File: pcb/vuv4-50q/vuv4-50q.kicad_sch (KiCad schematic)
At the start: 7 parts, among them J1 Conn_Coaxial, J2 Conn_Coaxial, J3 Conn_Coaxial, J4 Conn_Coaxial, J5 Conn_Coaxial, U1 SiPM

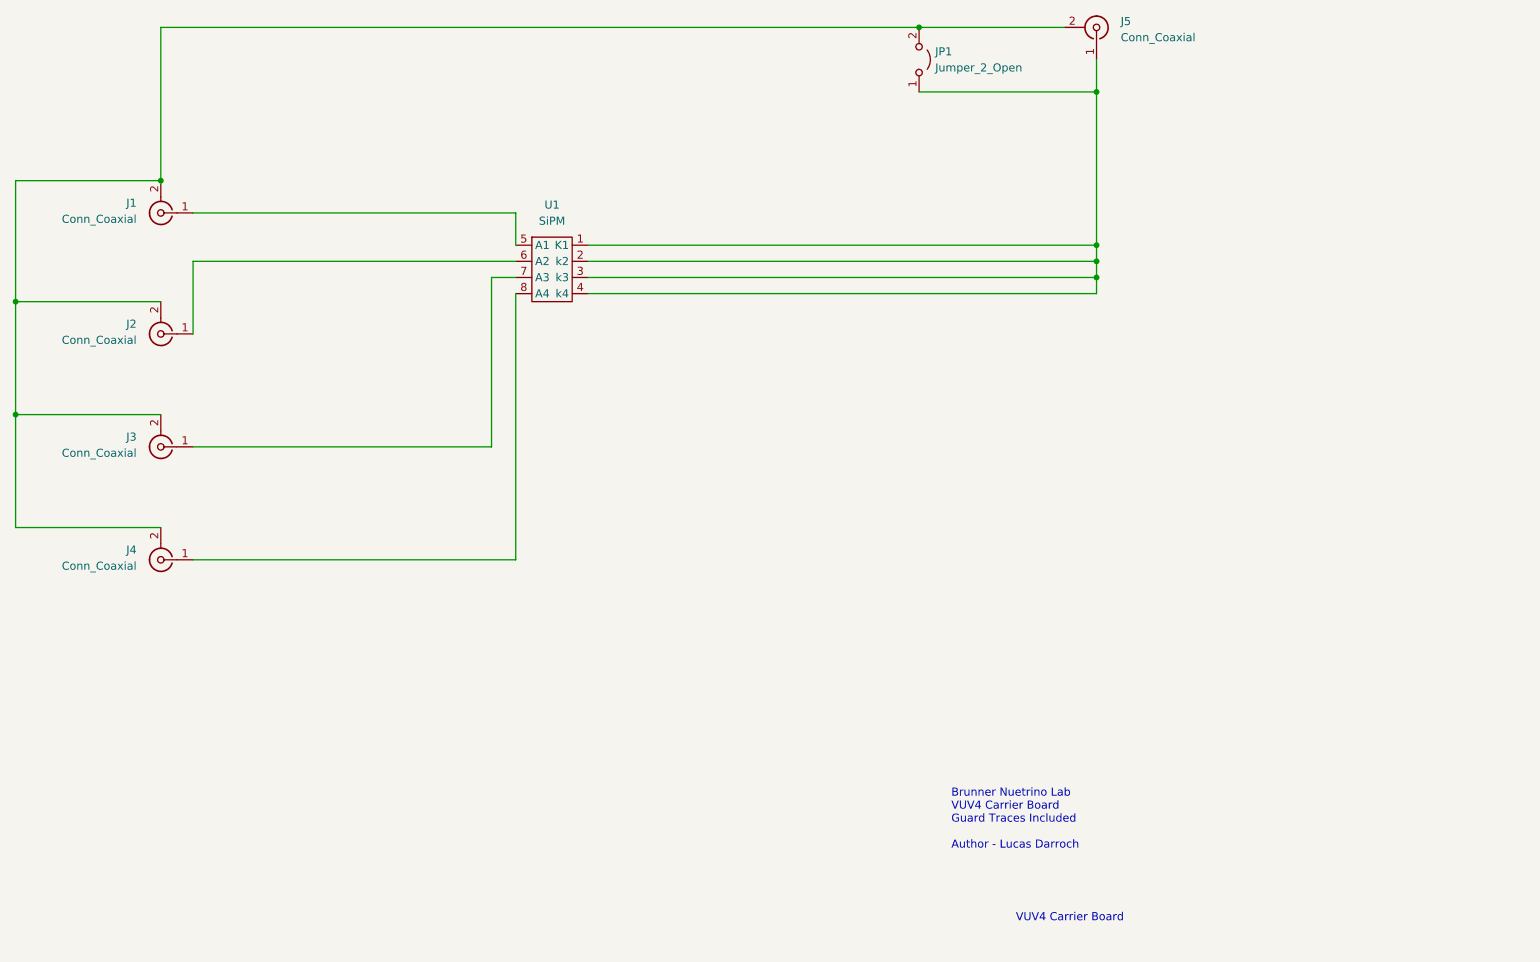
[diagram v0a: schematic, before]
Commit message: Added vuv4x3 - single vuv4 carrier board with u.fl connectors and passive summing
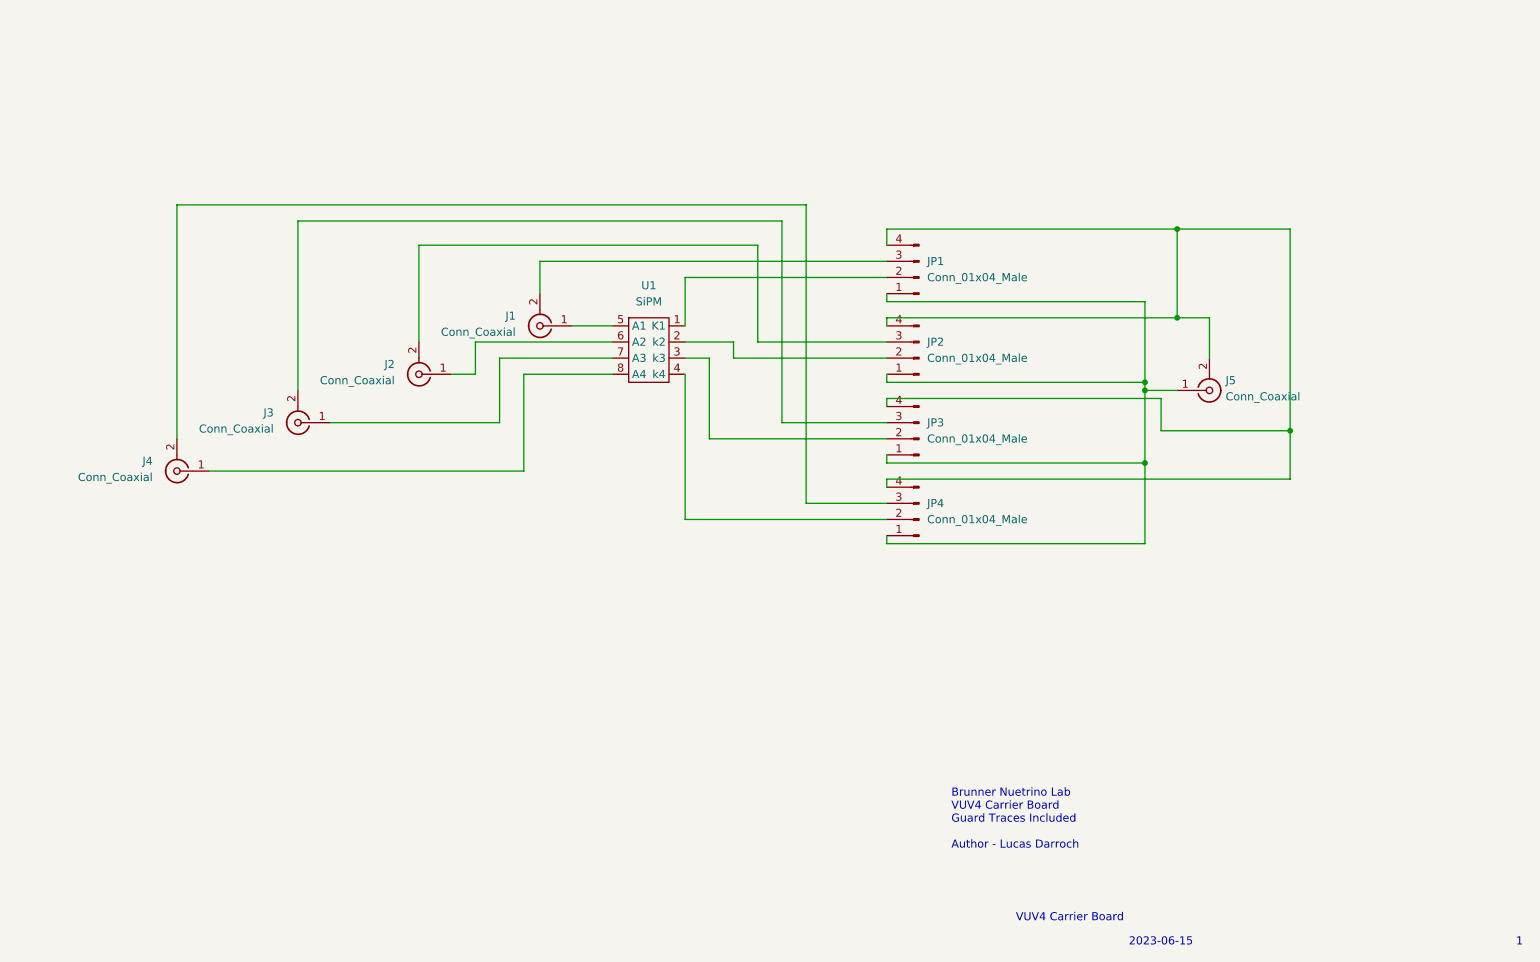
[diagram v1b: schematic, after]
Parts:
- removed JP1: Jumper_2_Open, Connector_PinHeader_2.54mm:PinHeader_1x02_P2.54mm_Vertical, symbol Jumper:Jumper_2_Open
- added JP1, JP2, JP3, JP4: Conn_01x04_Male, Connector_PinHeader_2.54mm:PinHeader_1x04_P2.54mm_Vertical, symbol Connector:Conn_01x04_Male
- J1, J2, J3, J4, J5: footprint vuv4x2:MCX_Vertical -> eec:Molex-0734152061-0
- U1: footprint vuv4x2:VUV4-50q -> Library:VUV4-50q
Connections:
- new net: J5.1 (In), JP1.1 (Pin_1), JP2.1 (Pin_1), JP3.1 (Pin_1), JP4.1 (Pin_1)
- new net: JP4.2 (Pin_2), U1.4 (k4)
- new net: J4.2 (Ext), JP4.3 (Pin_3)
- new net: J5.2 (Ext), JP1.4 (Pin_4), JP2.4 (Pin_4), JP3.4 (Pin_4), JP4.4 (Pin_4)
- new net: J3.2 (Ext), JP3.3 (Pin_3)
- new net: J1.2 (Ext), JP1.3 (Pin_3)
- new net: JP2.2 (Pin_2), U1.2 (k2)
- new net: J2.2 (Ext), JP2.3 (Pin_3)
- new net: JP1.2 (Pin_2), U1.1 (K1)
- new net: JP3.2 (Pin_2), U1.3 (k3)
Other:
- note added: "1"
- note added: "2023-06-15"
- moved on the sheet: J1, J2, J3, J4, U1
